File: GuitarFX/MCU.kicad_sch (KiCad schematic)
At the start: 42 parts, among them J301 USB_C_Receptacle_USB2.0, J302 Conn_ARM_SWD_TagConnect_TC2030, J303 Screw_Terminal_01x06, SW301 SW_SPDT, U2 STM32H733VGTx, U301 USBLC6-2SC6, Y301 24MHz

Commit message: SWD routing done
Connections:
- net SWCLK: now also D302.5 (K4); no longer D302.4 (K3)
- net SWDIO: now also D302.4 (K3); no longer D302.5 (K4)

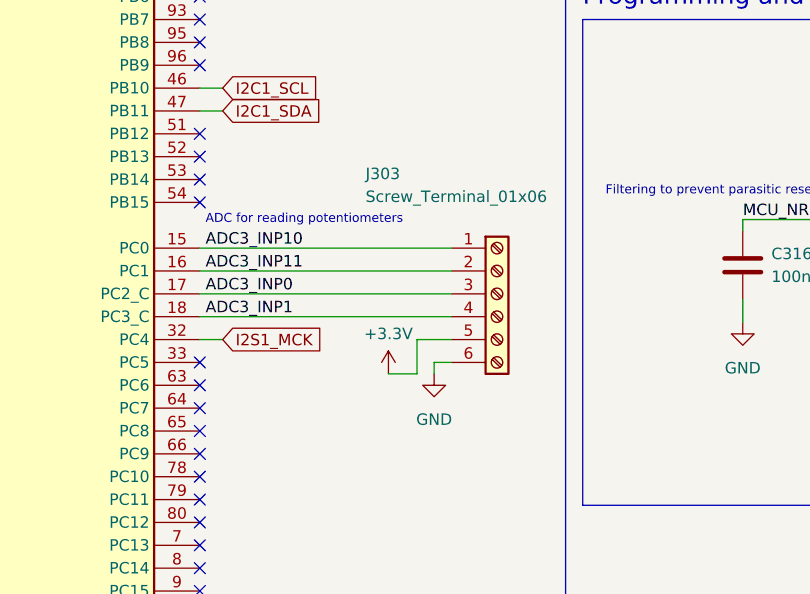
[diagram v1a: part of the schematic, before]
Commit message: Completed ADC terminal block connections. Finished routing
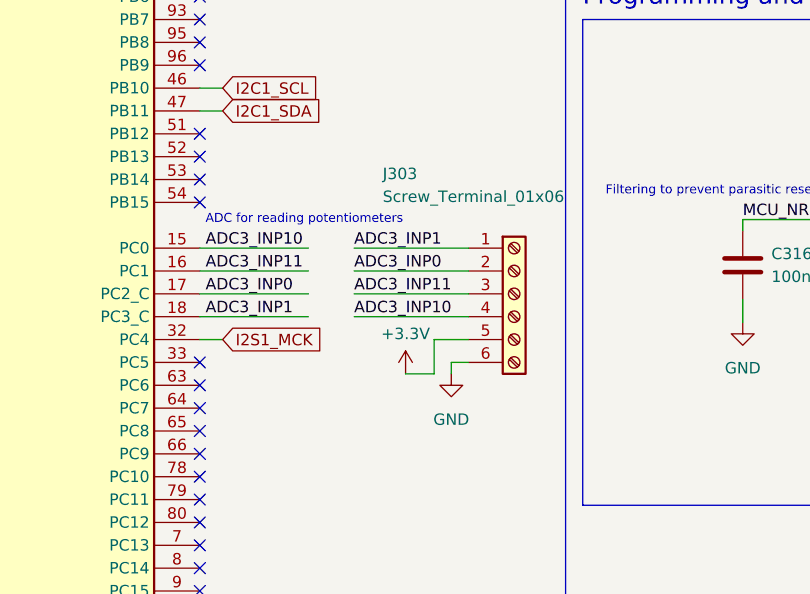
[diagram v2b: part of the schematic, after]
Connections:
- net ADC3_INP0: now also J303.2 (Pin_2); no longer J303.3 (Pin_3)
- net ADC3_INP1: now also J303.1 (Pin_1); no longer J303.4 (Pin_4)
- net ADC3_INP10: now also J303.4 (Pin_4); no longer J303.1 (Pin_1)
- net ADC3_INP11: now also J303.3 (Pin_3); no longer J303.2 (Pin_2)
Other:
- moved on the sheet: J303

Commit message: Added JLCPCB part numbers for main hardware components to order them
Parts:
- C314, C315: value 20p -> 14p
- D302: JLCPCB Part# (none) -> C3021133
- D303: JLCPCB Part# (none) -> C5547384
- FL301: JLCPCB Part# (none) -> C3211819
- J301: JLCPCB Part# (none) -> C165948
- J303: JLCPCB Part# (none) -> C3817456
- SW301: JLCPCB Part# (none) -> C221841
- U2: JLCPCB Part# (none) -> C730160
- U301: JLCPCB Part# (none) -> C5261088
- Y301: JLCPCB Part# (none) -> C5181479
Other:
- note added: "Cload = 2*(Co-Cs) Co = 12p Cs estimated to be 5p"
- note removed: "Cload = 2*(Co-Cs) Co = 15p Cs estimated to be 5p"
